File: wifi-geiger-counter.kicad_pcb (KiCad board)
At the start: 2 copper layers, 64 parts, among them J1 TYPE-C-31-M-12, J2 S2B-PH-K-S-GW, J3 SBM-20, Q1 MMBTA42_C8515, Q2 MMBT3904, Q3 MMBT3904, SW1 RESET, SW2 BOOT, U1 TP4056, U2 ESP32-C3-MINI-1-N4, U3 AP2112K-3.3TRG1, U4 USBLC6-2SC6

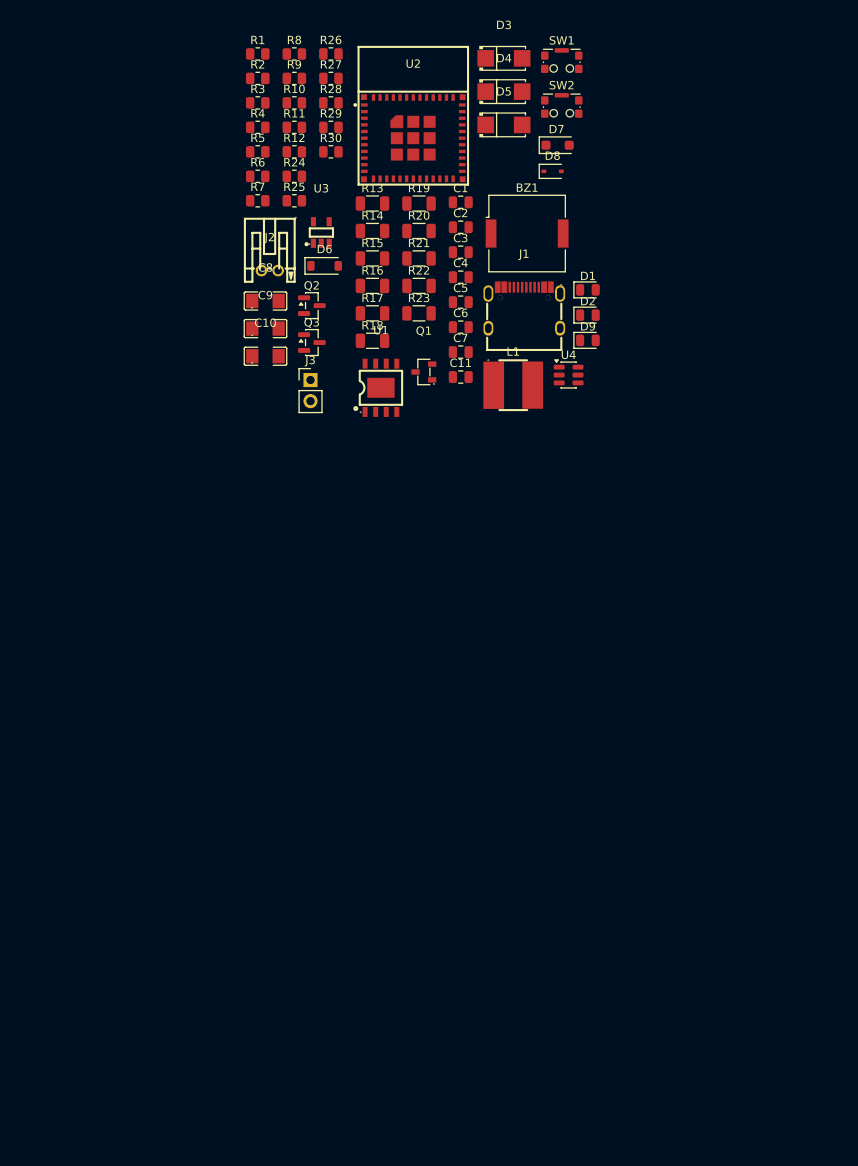
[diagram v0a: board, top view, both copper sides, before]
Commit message: PCB layout, placement, first routing, design rules
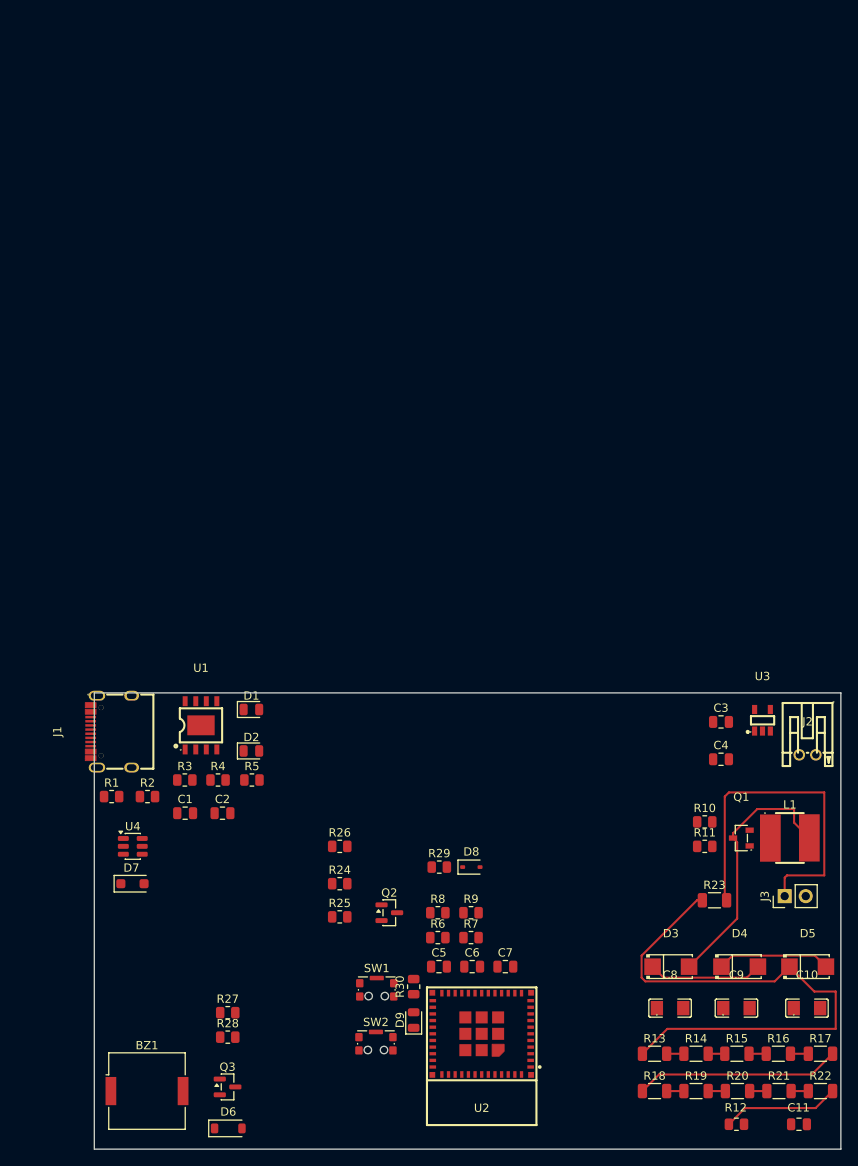
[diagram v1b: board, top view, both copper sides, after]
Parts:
- moved R12 128.8 mm to (129.4, 171.5)
- moved SW2 115.1 mm to (86.0, 161.8)
- moved SW1 114.0 mm to (86.0, 155.3)
- moved R27 113.3 mm to (68.1, 158.1)
- moved R28 113.3 mm to (68.1, 161.0)
- moved BZ1 113.1 mm to (58.4, 167.5)
- moved R19 112.1 mm to (124.5, 167.5)
- moved D3 111.3 mm to (121.5, 152.5)
- moved R20 110.6 mm to (129.5, 167.5)
- moved R21 109.4 mm to (134.5, 167.5)
- moved D4 109.2 mm to (129.8, 152.5)
- moved R22 108.5 mm to (139.5, 167.5)
- moved U2 108.3 mm to (98.7, 160.6), turned to 180 degrees
- moved R13 108.0 mm to (119.5, 163.0)
- moved D5 107.9 mm to (138.0, 152.5)
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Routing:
- net /HV: track 0.00 -> 67.3 mm
- net Net-(J3-Pin_1): track 0.00 -> 41.9 mm
- net /SW: track 0.00 -> 31.5 mm
- net Net-(R17-Pad2): track 0.00 -> 24.8 mm
- net /HV_FB: track 0.00 -> 14.2 mm
- net /HV1: track 0.00 -> 13.8 mm
- net /HV_X: track 0.00 -> 13.7 mm
- net Net-(R16-Pad2): track 0.00 -> 2.15 mm
- net Net-(R18-Pad2): track 0.00 -> 2.08 mm
- net Net-(R13-Pad2): track 0.00 -> 2.08 mm
- net Net-(R21-Pad2): track 0.00 -> 2.07 mm
- net Net-(R20-Pad2): track 0.00 -> 2.07 mm
- net Net-(R19-Pad2): track 0.00 -> 2.07 mm
- net Net-(R15-Pad2): track 0.00 -> 2.07 mm
- net Net-(R14-Pad2): track 0.00 -> 2.00 mm
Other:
- board outline added: 90 x 55 mm

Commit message: Most routing done
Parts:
- moved J1 1.21 mm to (55.2, 124.2)
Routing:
- net +3V3: track 0.00 -> 169.7 mm, vias 0 -> 7
- net /VBAT: track 0.00 -> 98.6 mm
- net /EN: track 0.00 -> 60.9 mm, vias 0 -> 5
- net /USB_DP: track 0.00 -> 60.5 mm, vias 0 -> 4
- net /HV_X: track 13.7 -> 70.7 mm
- net /USB_DN: track 0.00 -> 55.2 mm, vias 0 -> 4
- net /HV_FB: track 14.2 -> 61.1 mm, vias 0 -> 2
- net /VBUS: track 0.00 -> 45.7 mm, vias 0 -> 2
- net /IO2: track 0.00 -> 45.4 mm, vias 0 -> 5
- net /BUZZER: track 0.00 -> 40.9 mm, vias 0 -> 4
- net /PULSE_SAFE: track 0.00 -> 40.3 mm, vias 0 -> 4
- net Net-(J3-Pin_1): track 41.9 -> 7.21 mm
- net /BOOT: track 0.00 -> 30.2 mm, vias 0 -> 4
- net /HV1: track 13.8 -> 41.6 mm, vias 0 -> 2
- net /TUBE_K: track 0.00 -> 26.2 mm, vias 0 -> 2
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
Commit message: routing probably done, pre ground pour
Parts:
- moved U3 33.4 mm to (99.1, 122.4)
- moved C3 33.4 mm to (94.1, 122.6)
- moved C4 33.4 mm to (94.1, 127.1)
- moved J2 33.4 mm to (104.6, 126.6)
- moved R10 9.92 mm to (120.4, 126.6)
- moved Q1 9.92 mm to (124.8, 128.5)
- moved R11 9.92 mm to (120.4, 129.5)
- moved L1 9.92 mm to (130.7, 128.5)
- moved R23 9.50 mm to (119.6, 138.3)
- moved C8 7.11 mm to (116.5, 152.4), turned to 180 degrees
- moved J1 5.18 mm to (50.1, 125.1)
- moved D4 4.72 mm to (129.6, 147.8)
- moved D5 4.72 mm to (137.8, 147.8)
- moved C10 4.72 mm to (137.7, 152.8)
- moved C9 4.72 mm to (129.2, 152.8)
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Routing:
- net /BOOT: track 30.2 -> 119.2 mm, vias 4 -> 11
- net /TUBE_K: track 26.2 -> 107.7 mm
- net /HV_X: track 70.7 -> 26.9 mm, vias 0 -> 3
- net Net-(U2-IO8): track 0.00 -> 34.4 mm, vias 0 -> 6
- net Net-(D1-K): track 6.91 -> 40.4 mm, vias 0 -> 2
- net /SW: track 27.9 -> 59.0 mm, vias 0 -> 3
- net /USB_DN: track 55.2 -> 85.0 mm, vias 4 -> 6
- net /USB_DP: track 60.5 -> 84.8 mm, vias 4 -> 7
- net /HV_PWM: track 18.1 -> 41.6 mm, vias 1 -> 2
- net /VBUS: track 45.7 -> 65.8 mm, vias 2 -> 6
- net +3V3: track 169.7 -> 151.3 mm, vias 7 -> 6
- net /HV1: track 41.6 -> 25.1 mm, vias 2 -> 0
- net /VBAT: track 98.6 -> 115.0 mm, vias 0 -> 3
- net Net-(J1-CC2): track 0.00 -> 15.9 mm
- net Net-(J1-CC1): track 0.00 -> 15.7 mm
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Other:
- board size 90 x 55 mm -> 95 x 55 mm

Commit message: finish pour and clear warnings and errors, cleanup, routing done.
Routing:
- net GND: track 0.00 -> 16.7 mm, vias 0 -> 8
- added copper zone on B.Cu, net GND
- added copper zone on F.Cu, net GND
